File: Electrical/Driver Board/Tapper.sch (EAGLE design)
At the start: 38 parts, among them M0 B2B-PH-K, M1 B2B-PH-K, M2 B2B-PH-K, M3 B2B-PH-K, M4 B2B-PH-K, M5 B2B-PH-K, M6 B2B-PH-K, M7 B2B-PH-K, P1 B5B-PH-K, P2 B4B-PH-K, U10 DRV2605LDGS, U11 DRV2605LDGS, U12 TCA9548APWR | PCA9548APW,118 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, U3 DRV2605LDGS, U4 DRV2605LDGS, U5 DRV2605LDGS, U6 DRV2605LDGS, U7 DRV2605LDGS, U8 DRV2605LDGS, U9 DRV2605LDGS

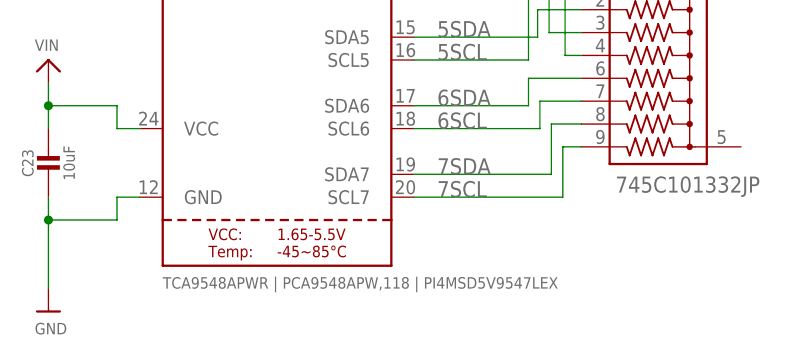
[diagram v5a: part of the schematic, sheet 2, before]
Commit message: i2c bus chip PI4MSD5V9547LEX is NOT the same as TCA9548APWR. It may be made to run similar, but, for instance, it has a different control register that doesnt allow for simultaneous writing to multiple busses
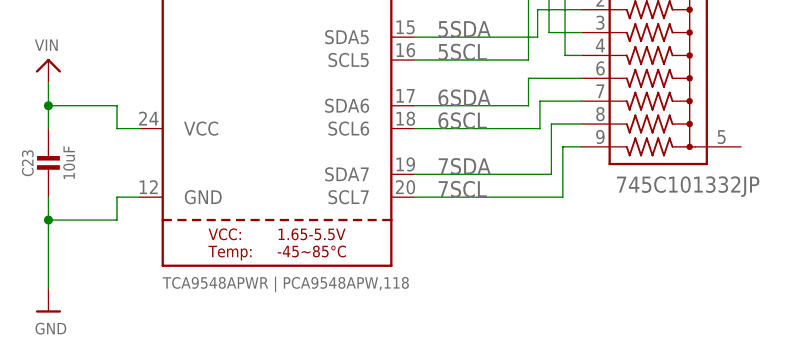
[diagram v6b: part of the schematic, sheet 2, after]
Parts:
- U12: value TCA9548APWR | PCA9548APW,118 | PI4MSD5V9547LEX -> TCA9548APWR | PCA9548APW,118
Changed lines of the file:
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@@
 <part name="U$63" library="microbuilder" deviceset="GND" device=""/>
 <part name="U$65" library="microbuilder" deviceset="FRAME_A4_ADAFRUIT" device=""/>
-<part name="U12" library="microbuilder" deviceset="TCA9548A" device="" value=" TCA9548APWR | PCA9548APW,118 | PI4MSD5V9547LEX"/>
+<part name="U12" library="microbuilder" deviceset="TCA9548A" device="" value=" TCA9548APWR | PCA9548APW,118"/>
 <part name="R5" library="microbuilder" deviceset="RESISTOR" device="0805_NOOUTLINE" value="10K"/>
 <part name="R6" library="microbuilder" deviceset="RESISTOR" device="0805_NOOUTLINE" value="10K"/>

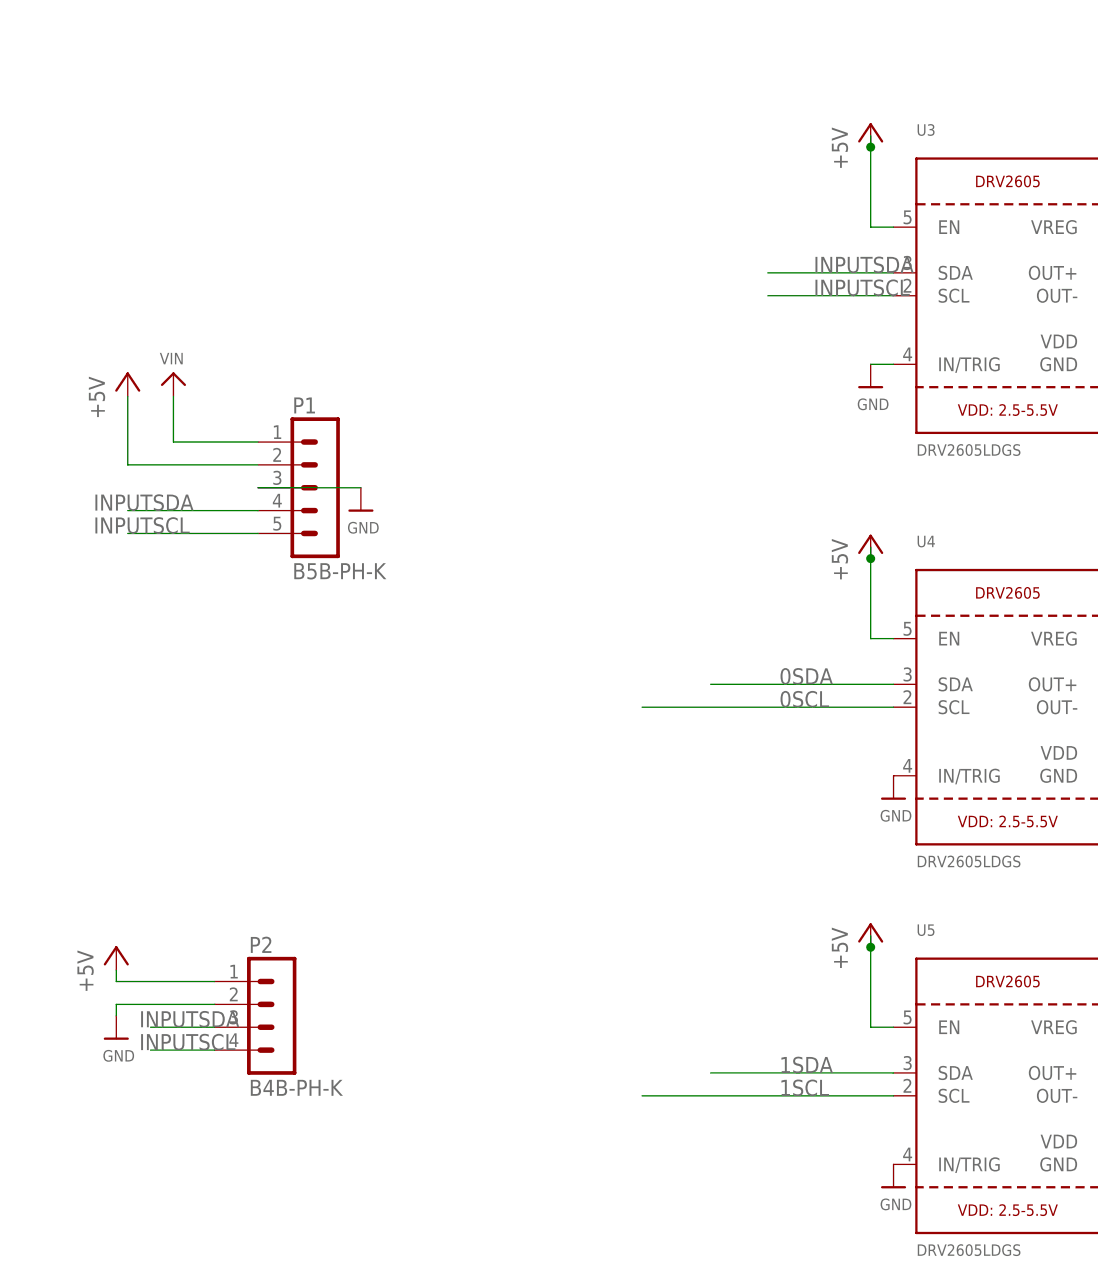
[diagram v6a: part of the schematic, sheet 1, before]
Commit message: 0.32: Add 3v3 reg, remove disp, add buffer for (hopefully) enabling the lone driver
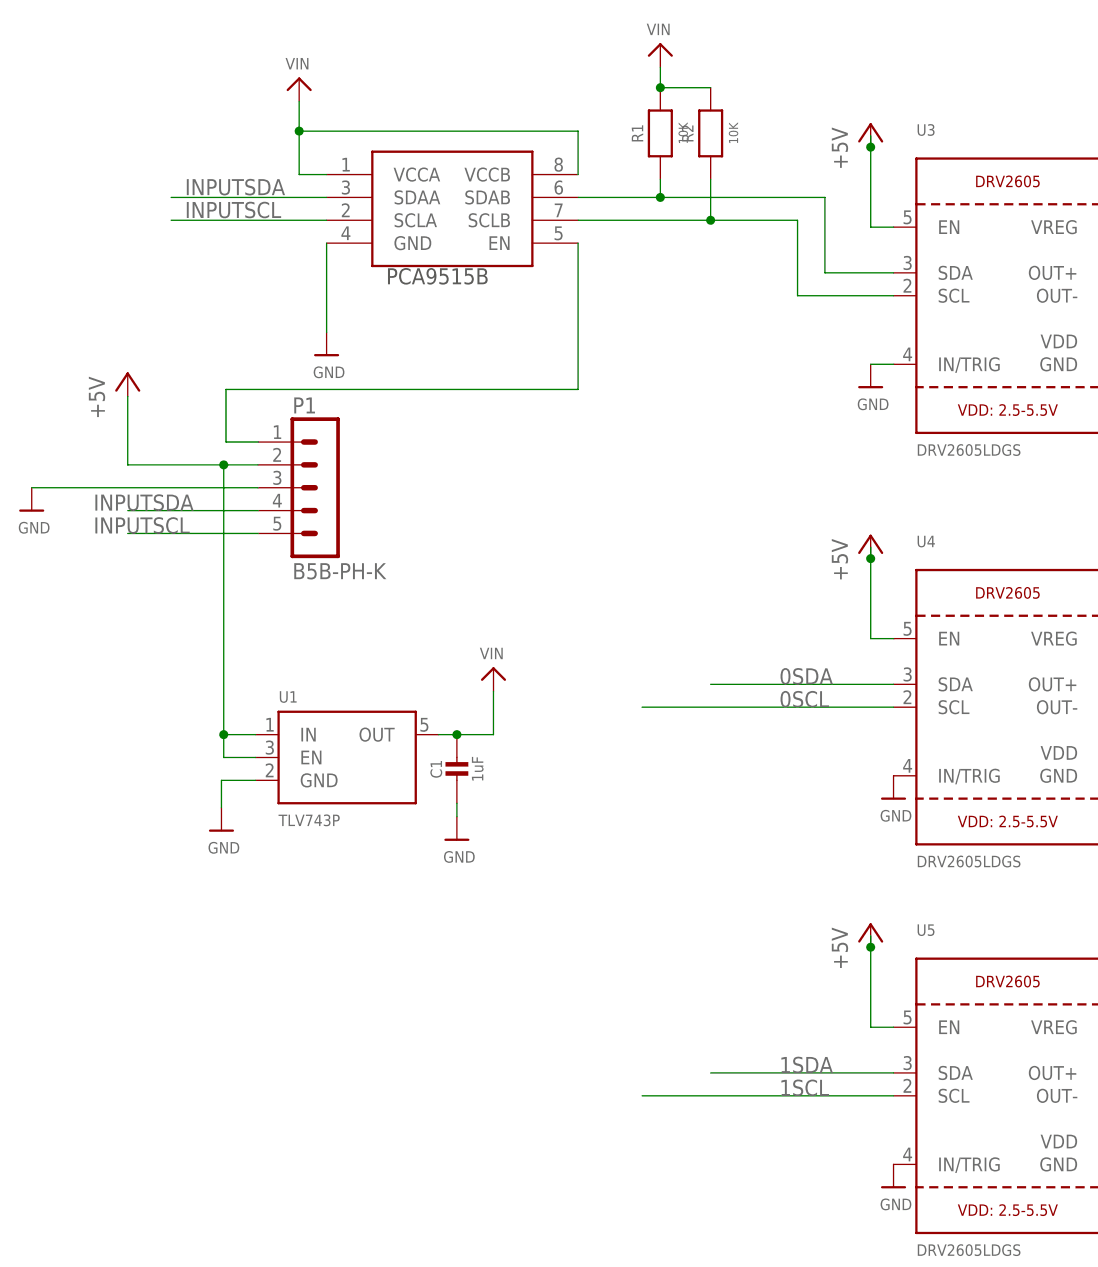
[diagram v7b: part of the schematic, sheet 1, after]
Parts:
- removed P2: B4B-PH-K, con-jst-ph:B4B-PH-K
- added C1: 1uF, microbuilder:CAP_CERAMIC0805-NOOUTLINE
- added R1, R2: 10K, microbuilder:RESISTOR0805_NOOUTLINE
- added U1: TLV743P, microbuilder:LD39015XX
- added U23: PCA9515B, PCA9517:PCA9517
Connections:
- new net N$12: R1.1, U23.SDAB, U3.SDA
- new net N$13: R2.1, U23.SCLB, U3.SCL
- new net N$5: P1.1, U23.EN
- net +5V: now also U1.EN, U1.IN; no longer P2.1
- net GND: now also C1.2, U1.GND, U23.GND; no longer P2.2
- net INPUTSCL: now also U23.SCLA; no longer P2.4, U3.SCL
- net INPUTSDA: now also U23.SDAA; no longer P2.3, U3.SDA
- net VIN: now also C1.1, R1.2, R2.2, U1.OUT, U23.VCCA, U23.VCCB; no longer P1.1
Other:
- note added: "PCA9515B"

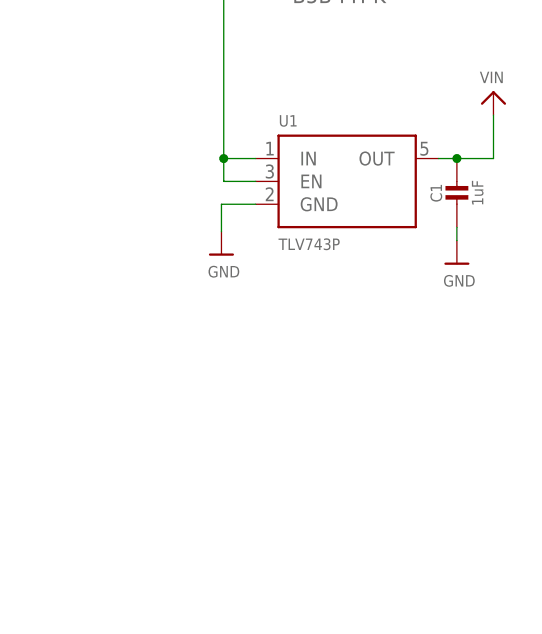
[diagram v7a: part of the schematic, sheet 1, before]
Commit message: Add power led
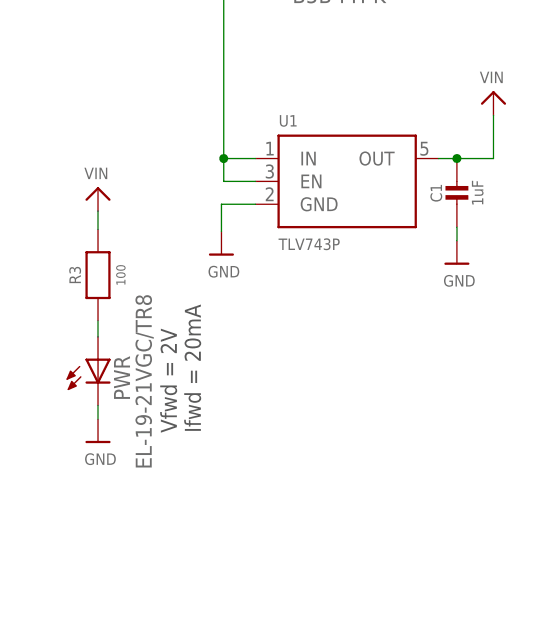
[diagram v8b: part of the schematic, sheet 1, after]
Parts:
- added PWR: EL-19-21VGC/TR8, adafruit:LEDCHIP-LED0603
- added R3: 100, microbuilder:RESISTOR0805_NOOUTLINE
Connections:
- new net N$14: PWR.A, R3.1
- net GND: now also PWR.C
- net VIN: now also R3.2
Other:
- note added: "Vfwd = 2V Ifwd = 20mA"
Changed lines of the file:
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@@
 <part name="V3.2" library="microbuilder" deviceset="VIN" device=""/>
 <part name="V3.3" library="microbuilder" deviceset="VIN" device=""/>
+<part name="PWR" library="adafruit" library_urn="urn:adsk.eagle:library:420" deviceset="LED" device="CHIP-LED0603" package3d_urn="urn:adsk.eagle:package:6240556/1" value="EL-19-21VGC/TR8"/>
+<part name="R3" library="microbuilder" deviceset="RESISTOR" device="0805_NOOUTLINE" value="100"/>
+<part name="U$8" library="microbuilder" deviceset="GND" device=""/>
+<part name="V3.4" library="microbuilder" deviceset="VIN" device=""/>
 </parts>
 <sheets>
@@
 <plain>
 <text x="50.292" y="138.43" size="1.778" layer="97">PCA9515B</text>
+<text x="29.718" y="57.912" size="1.778" layer="97" rot="R90">Vfwd = 2V
+Ifwd = 20mA</text>
 </plain>
 <instances>
@@
 <instance part="V3.3" gate="G$1" x="62.23" y="95.758" smashed="yes">
 <attribute name="VALUE" x="60.706" y="96.774" size="1.27" layer="96"/>
+</instance>
+<instance part="PWR" gate="G$1" x="18.288" y="66.04" smashed="yes">
+<attribute name="NAME" x="21.844" y="61.468" size="1.778" layer="95" rot="R90"/>
+<attribute name="VALUE" x="24.257" y="53.848" size="1.778" layer="96" rot="R90"/>
+</instance>
+<instance part="R3" gate="G$1" x="18.288" y="75.438" smashed="yes" rot="R90">
+<attribute name="NAME" x="15.748" y="75.438" size="1.27" layer="95" font="vector" rot="R90" align="center"/>
+<attribute name="VALUE" x="20.828" y="75.438" size="1.016" layer="96" font="vector" ratio="15" rot="R90" align="center"/>
+</instance>
+<instance part="U$8" gate="G$1" x="18.288" y="56.896" smashed="yes">
+<attribute name="VALUE" x="16.764" y="54.356" size="1.27" layer="96"/>
+</instance>
+<instance part="V3.4" gate="G$1" x="18.288" y="85.09" smashed="yes">
+<attribute name="VALUE" x="16.764" y="86.106" size="1.27" layer="96"/>
 </instance>
 </instances>
@@
 <junction x="80.772" y="160.274"/>
 </segment>
+<segment>
+<pinref part="V3.4" gate="G$1" pin="VIN"/>
+<pinref part="R3" gate="G$1" pin="2"/>
+<wire x1="18.288" y1="82.55" x2="18.288" y2="80.518" width="0.1524" layer="91"/>
+</segment>
 </net>
 <net name="GND" class="1">
@@
 <pinref part="U$24" gate="G$1" pin="GND"/>
 <wire x1="58.166" y1="80.772" x2="58.166" y2="79.248" width="0.1524" layer="91"/>
+</segment>
+<segment>
+<pinref part="PWR" gate="G$1" pin="C"/>
+<pinref part="U$8" gate="G$1" pin="GND"/>
+<wire x1="18.288" y1="60.96" x2="18.288" y2="59.436" width="0.1524" layer="91"/>
 </segment>
 </net>
@@
 <wire x1="86.36" y1="150.114" x2="86.36" y2="145.542" width="0.1524" layer="91"/>
 <junction x="86.36" y="145.542"/>
+</segment>
+</net>
+<net name="N$14" class="0">
+<segment>
+<pinref part="R3" gate="G$1" pin="1"/>
+<pinref part="PWR" gate="G$1" pin="A"/>
+<wire x1="18.288" y1="70.358" x2="18.288" y2="68.58" width="0.1524" layer="91"/>
 </segment>
 </net>
@@
 with this version.
 </note>
+<note version="8.3" severity="warning">
+Since Version 8.3, EAGLE supports URNs for individual library
+assets (packages, symbols, and devices). The URNs of those assets
+will not be understood (or retained) with this version.
+</note>
+<note version="8.3" severity="warning">
+Since Version 8.3, EAGLE supports the association of 3D packages
+with devices in libraries, schematics, and board files. Those 3D
+packages will not be understood (or retained) with this version.
+</note>
 </compatibility>
